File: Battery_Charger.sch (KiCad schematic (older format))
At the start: 27 parts

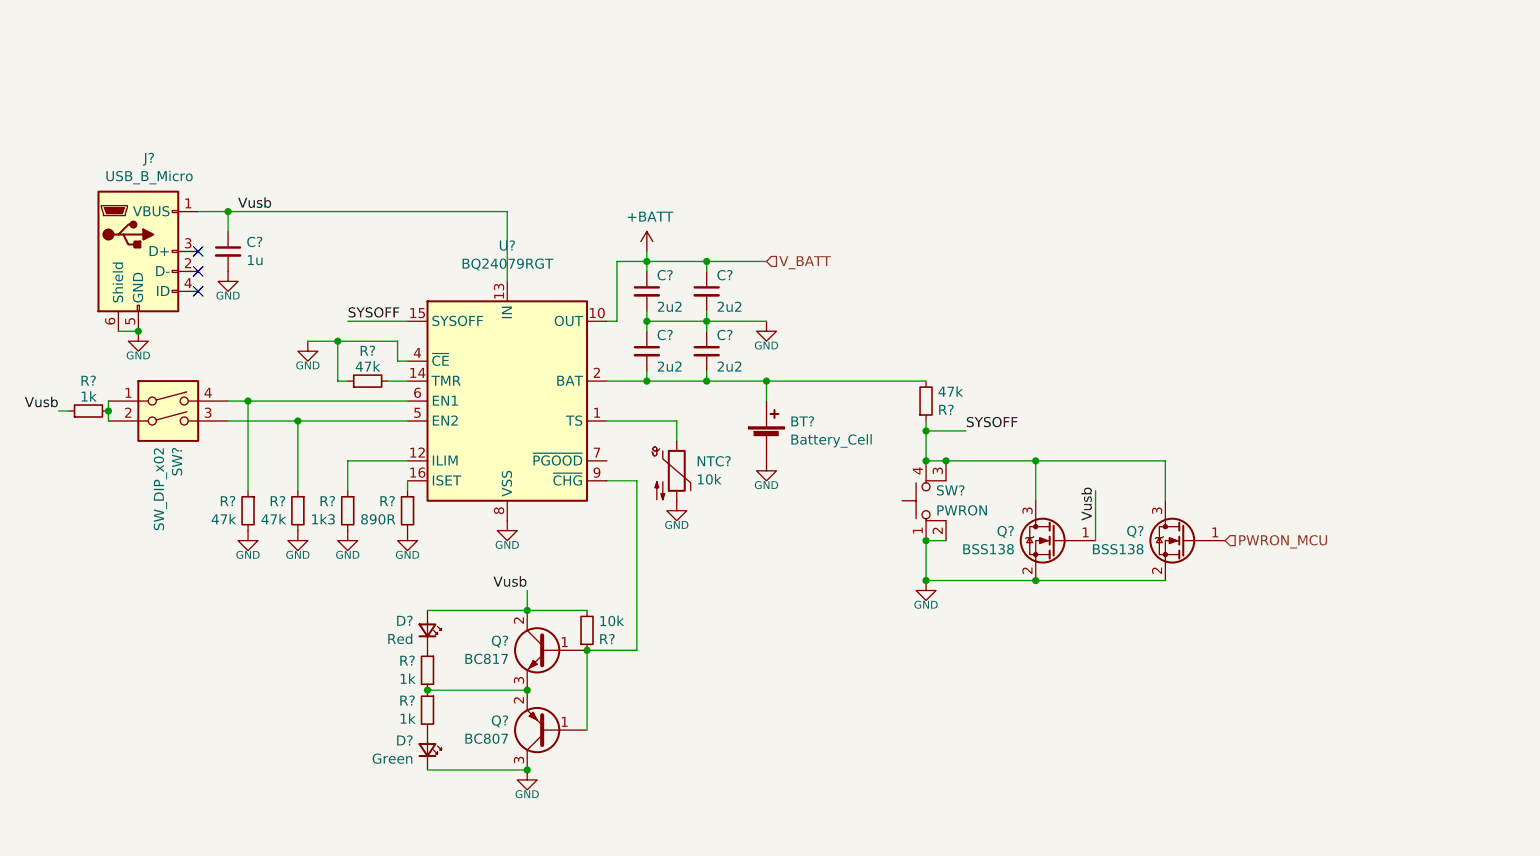
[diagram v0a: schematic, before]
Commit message: - supply converter develop - added sheet: MCU - cleanup 'koncepcja' sub-schematics
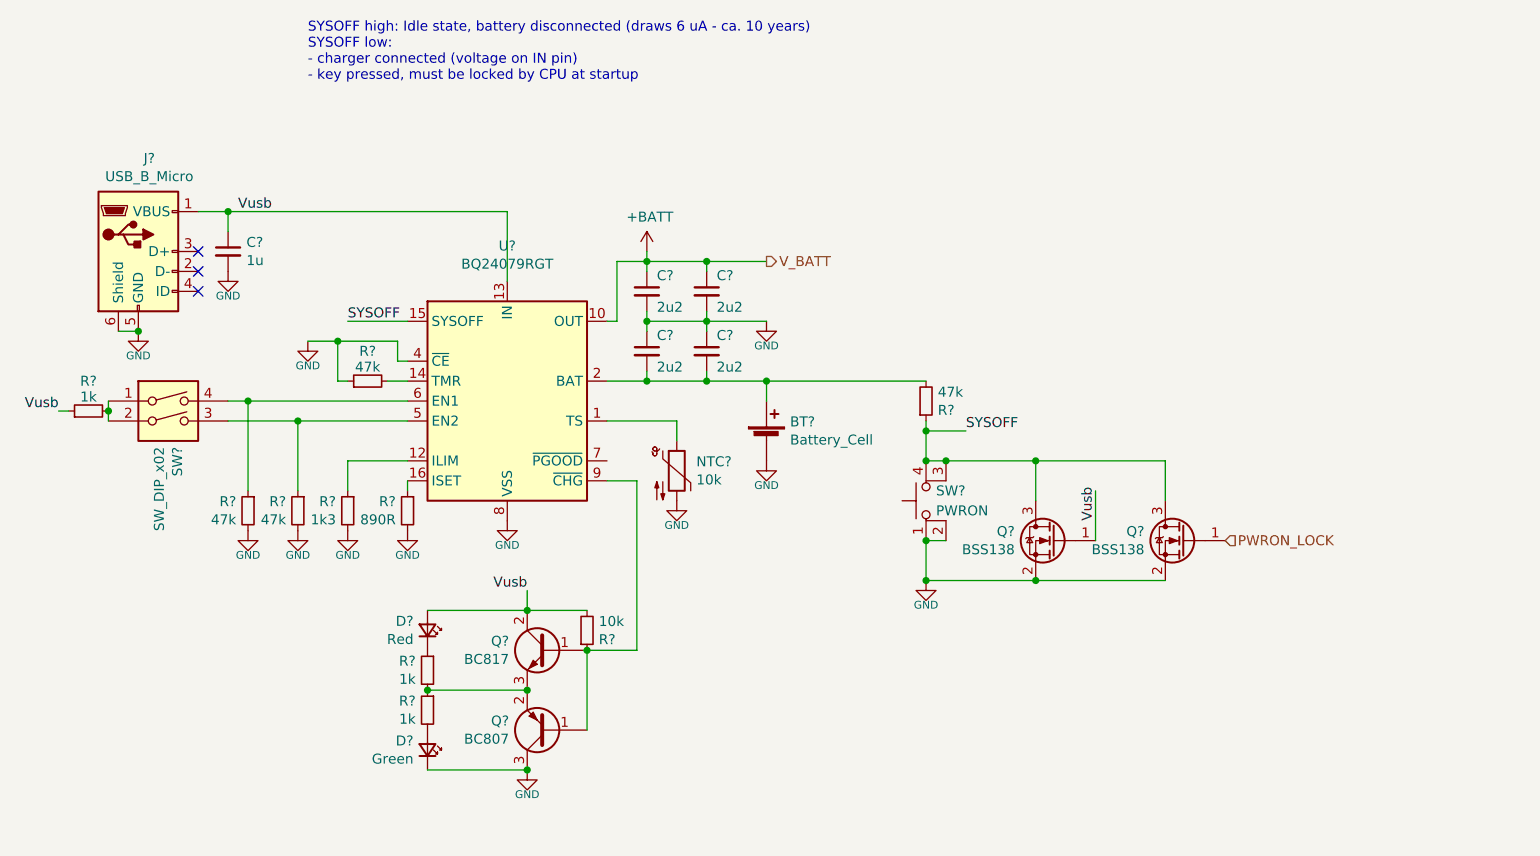
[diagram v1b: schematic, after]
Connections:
- net PWRON_MCU renamed PWRON_LOCK
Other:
- note added: "SYSOFF high: Idle state, battery disconnected (draws 6 uA - ca. 10 years)\nSYSOFF low:\n- charger connected (voltage on IN pin)\n- key pressed, must be locked by CPU at startup"
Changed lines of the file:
@@
 $Descr A4 11693 8268
 encoding utf-8
-Sheet 10 10
+Sheet 10 9
 Title ""
 Date ""
@@
 U 1 1 5F7AA8B0
 P 6150 3600
+AR Path="/5F620813/5F7AA8B0" Ref="BT?"  Part="1"
+AR Path="/5F7A93EE/5F7AA8B0" Ref="BT?"  Part="1"
 F 0 "BT?" H 6268 3696 50  0000 L CNN
 F 1 "Battery_Cell" H 6268 3605 50  0000 L CNN
@@
 U 1 1 5F7AA8B7
 P 4850 3400
+AR Path="/5F620813/5F7AA8B7" Ref="U?"  Part="1"
+AR Path="/5F7A93EE/5F7AA8B7" Ref="U?"  Part="1"
 F 0 "U?" H 4850 4178 50  0000 C CNN
 F 1 "BQ24079RGT" H 4850 4087 50  0000 C CNN
@@
 U 1 1 5F7AA8BE
 P 3000 2650
+AR Path="/5F620813/5F7AA8BE" Ref="J?"  Part="1"
+AR Path="/5F7A93EE/5F7AA8BE" Ref="J?"  Part="1"
 F 0 "J?" H 3055 3117 50  0000 C CNN
 F 1 "USB_B_Micro" H 3055 3026 50  0000 C CNN
@@
 AR Path="/5F7AA8C5" Ref="#PWR?"  Part="1"
 AR Path="/5F620813/5F7AA8C5" Ref="#PWR?"  Part="1"
+AR Path="/5F7A93EE/5F7AA8C5" Ref="#PWR?"  Part="1"
 F 0 "#PWR?" H 3000 2890 50  0001 C CNN
 F 1 "GND" H 3000 2950 39  0000 C TNN
@@
 U 1 1 5F7AA8D1
 P 3450 2650
+AR Path="/5F620813/5F7AA8D1" Ref="C?"  Part="1"
+AR Path="/5F7A93EE/5F7AA8D1" Ref="C?"  Part="1"
 F 0 "C?" H 3542 2696 50  0000 L CNN
 F 1 "1u" H 3542 2605 50  0000 L CNN
@@
 AR Path="/5F7AA8D8" Ref="#PWR?"  Part="1"
 AR Path="/5F620813/5F7AA8D8" Ref="#PWR?"  Part="1"
+AR Path="/5F7A93EE/5F7AA8D8" Ref="#PWR?"  Part="1"
 F 0 "#PWR?" H 3450 2590 50  0001 C CNN
 F 1 "GND" H 3450 2650 39  0000 C TNN
@@
 U 1 1 5F7AA8E8
 P 4450 4550
+AR Path="/5F620813/5F7AA8E8" Ref="D?"  Part="1"
+AR Path="/5F7A93EE/5F7AA8E8" Ref="D?"  Part="1"
 F 0 "D?" V 4496 4480 50  0000 R CNN
 F 1 "Red" V 4405 4480 50  0000 R CNN
@@
 AR Path="/5F7AA8F0" Ref="#PWR?"  Part="1"
 AR Path="/5F620813/5F7AA8F0" Ref="#PWR?"  Part="1"
+AR Path="/5F7A93EE/5F7AA8F0" Ref="#PWR?"  Part="1"
 F 0 "#PWR?" H 4850 3840 50  0001 C CNN
 F 1 "GND" H 4850 3900 39  0000 C TNN
@@
 AR Path="/5F7AA8F6" Ref="#PWR?"  Part="1"
 AR Path="/5F620813/5F7AA8F6" Ref="#PWR?"  Part="1"
+AR Path="/5F7A93EE/5F7AA8F6" Ref="#PWR?"  Part="1"
 F 0 "#PWR?" H 6150 3540 50  0001 C CNN
 F 1 "GND" H 6150 3600 39  0000 C TNN
@@
 AR Path="/5F7AA8FC" Ref="#PWR?"  Part="1"
 AR Path="/5F620813/5F7AA8FC" Ref="#PWR?"  Part="1"
+AR Path="/5F7A93EE/5F7AA8FC" Ref="#PWR?"  Part="1"
 F 0 "#PWR?" H 3850 2940 50  0001 C CNN
 F 1 "GND" H 3850 3000 39  0000 C TNN
@@
 U 1 1 5F7AA902
 P 3150 3500
+AR Path="/5F620813/5F7AA902" Ref="SW?"  Part="1"
+AR Path="/5F7A93EE/5F7AA902" Ref="SW?"  Part="1"
 F 0 "SW?" V 3196 3370 50  0000 R CNN
 F 1 "SW_DIP_x02" V 3105 3370 50  0000 R CNN
@@
 U 1 1 5F7AA90A
 P 4450 5150
+AR Path="/5F620813/5F7AA90A" Ref="D?"  Part="1"
+AR Path="/5F7A93EE/5F7AA90A" Ref="D?"  Part="1"
 F 0 "D?" V 4496 5080 50  0000 R CNN
 F 1 "Green" V 4405 5080 50  0000 R CNN
@@
 U 1 1 5F7AA911
 P 5050 5050
+AR Path="/5F620813/5F7AA911" Ref="Q?"  Part="1"
+AR Path="/5F7A93EE/5F7AA911" Ref="Q?"  Part="1"
 F 0 "Q?" H 5241 5004 50  0000 L CNN
 F 1 "BC807" H 5241 5095 50  0000 L CNN
@@
 U 1 1 5F7AA918
 P 5050 4650
+AR Path="/5F620813/5F7AA918" Ref="Q?"  Part="1"
+AR Path="/5F7A93EE/5F7AA918" Ref="Q?"  Part="1"
 F 0 "Q?" H 5241 4696 50  0000 L CNN
 F 1 "BC817" H 5241 4605 50  0000 L CNN
@@
 AR Path="/5F7AA920" Ref="#PWR?"  Part="1"
 AR Path="/5F620813/5F7AA920" Ref="#PWR?"  Part="1"
+AR Path="/5F7A93EE/5F7AA920" Ref="#PWR?"  Part="1"
 F 0 "#PWR?" H 4950 5090 50  0001 C CNN
 F 1 "GND" H 4950 5150 39  0000 C TNN
@@
 U 1 1 5F7AA927
 P 5250 4550
+AR Path="/5F620813/5F7AA927" Ref="R?"  Part="1"
+AR Path="/5F7A93EE/5F7AA927" Ref="R?"  Part="1"
 F 0 "R?" H 5309 4596 50  0000 L CNN
 F 1 "10k" H 5309 4505 50  0000 L CNN
@@
 AR Path="/5F7AA93D" Ref="#PWR?"  Part="1"
 AR Path="/5F620813/5F7AA93D" Ref="#PWR?"  Part="1"
+AR Path="/5F7A93EE/5F7AA93D" Ref="#PWR?"  Part="1"
 F 0 "#PWR?" H 4350 3890 50  0001 C CNN
 F 1 "GND" H 4350 3950 39  0000 C TNN
@@
 AR Path="/5F7AA943" Ref="#PWR?"  Part="1"
 AR Path="/5F620813/5F7AA943" Ref="#PWR?"  Part="1"
+AR Path="/5F7A93EE/5F7AA943" Ref="#PWR?"  Part="1"
 F 0 "#PWR?" H 4050 3890 50  0001 C CNN
 F 1 "GND" H 4050 3950 39  0000 C TNN
@@
 AR Path="/5F7AA94B" Ref="#PWR?"  Part="1"
 AR Path="/5F620813/5F7AA94B" Ref="#PWR?"  Part="1"
+AR Path="/5F7A93EE/5F7AA94B" Ref="#PWR?"  Part="1"
 F 0 "#PWR?" H 3800 3890 50  0001 C CNN
 F 1 "GND" H 3800 3950 39  0000 C TNN
@@
 U 1 1 5F7AA951
 P 3550 3950
+AR Path="/5F620813/5F7AA951" Ref="R?"  Part="1"
+AR Path="/5F7A93EE/5F7AA951" Ref="R?"  Part="1"
 F 0 "R?" H 3609 3996 50  0000 L CNN
 F 1 "47k" H 3609 3905 50  0000 L CNN
@@
 AR Path="/5F7AA958" Ref="#PWR?"  Part="1"
 AR Path="/5F620813/5F7AA958" Ref="#PWR?"  Part="1"
+AR Path="/5F7A93EE/5F7AA958" Ref="#PWR?"  Part="1"
 F 0 "#PWR?" H 3550 3890 50  0001 C CNN
 F 1 "GND" H 3550 3950 39  0000 C TNN
@@
 U 1 1 5F7AA968
 P 3800 3950
+AR Path="/5F620813/5F7AA968" Ref="R?"  Part="1"
+AR Path="/5F7A93EE/5F7AA968" Ref="R?"  Part="1"
 F 0 "R?" H 3859 3996 50  0000 L CNN
 F 1 "47k" H 3859 3905 50  0000 L CNN
@@
 U 1 1 5F7AA96F
 P 4050 3950
+AR Path="/5F620813/5F7AA96F" Ref="R?"  Part="1"
+AR Path="/5F7A93EE/5F7AA96F" Ref="R?"  Part="1"
 F 0 "R?" H 4109 3996 50  0000 L CNN
 F 1 "1k3" H 4109 3905 50  0000 L CNN
@@
 U 1 1 5F7AA976
 P 4350 3950
+AR Path="/5F620813/5F7AA976" Ref="R?"  Part="1"
+AR Path="/5F7A93EE/5F7AA976" Ref="R?"  Part="1"
 F 0 "R?" H 4409 3996 50  0000 L CNN
 F 1 "890R" H 4409 3905 50  0000 L CNN
@@
 U 1 1 5F7AA97D
 P 4450 4750
+AR Path="/5F620813/5F7AA97D" Ref="R?"  Part="1"
+AR Path="/5F7A93EE/5F7AA97D" Ref="R?"  Part="1"
 F 0 "R?" H 4509 4796 50  0000 L CNN
 F 1 "1k" H 4509 4705 50  0000 L CNN
@@
 U 1 1 5F7AA984
 P 4450 4950
+AR Path="/5F620813/5F7AA984" Ref="R?"  Part="1"
+AR Path="/5F7A93EE/5F7AA984" Ref="R?"  Part="1"
 F 0 "R?" H 4509 4996 50  0000 L CNN
 F 1 "1k" H 4509 4905 50  0000 L CNN
@@
 U 1 1 5F7AA98C
 P 2750 3450
+AR Path="/5F620813/5F7AA98C" Ref="R?"  Part="1"
+AR Path="/5F7A93EE/5F7AA98C" Ref="R?"  Part="1"
 F 0 "R?" V 2900 3450 50  0000 C CNN
 F 1 "1k" V 2850 3450 50  0000 C BNN
@@
 U 1 1 5F7AA998
 P 5700 3750
+AR Path="/5F620813/5F7AA998" Ref="NTC?"  Part="1"
+AR Path="/5F7A93EE/5F7AA998" Ref="NTC?"  Part="1"
 F 0 "NTC?" H 5798 3796 50  0000 L CNN
 F 1 "10k" H 5798 3705 50  0000 L CNN
@@
 AR Path="/5F7AA9A1" Ref="#PWR?"  Part="1"
 AR Path="/5F620813/5F7AA9A1" Ref="#PWR?"  Part="1"
+AR Path="/5F7A93EE/5F7AA9A1" Ref="#PWR?"  Part="1"
 F 0 "#PWR?" H 5700 3740 50  0001 C CNN
 F 1 "GND" H 5700 3800 39  0000 C TNN
@@
 U 1 1 5F7AA9A7
 P 5550 3150
+AR Path="/5F620813/5F7AA9A7" Ref="C?"  Part="1"
+AR Path="/5F7A93EE/5F7AA9A7" Ref="C?"  Part="1"
 F 0 "C?" H 5600 3200 50  0000 L BNN
 F 1 "2u2" H 5600 3100 50  0000 L TNN
@@
 U 1 1 5F7AA9AE
 P 5550 2850
+AR Path="/5F620813/5F7AA9AE" Ref="C?"  Part="1"
+AR Path="/5F7A93EE/5F7AA9AE" Ref="C?"  Part="1"
 F 0 "C?" H 5600 2900 50  0000 L BNN
 F 1 "2u2" H 5600 2800 50  0000 L TNN
@@
 U 1 1 5F7AA9B5
 P 5850 3150
+AR Path="/5F620813/5F7AA9B5" Ref="C?"  Part="1"
+AR Path="/5F7A93EE/5F7AA9B5" Ref="C?"  Part="1"
 F 0 "C?" H 5900 3200 50  0000 L BNN
 F 1 "2u2" H 5900 3100 50  0000 L TNN
@@
 U 1 1 5F7AA9BC
 P 5850 2850
+AR Path="/5F620813/5F7AA9BC" Ref="C?"  Part="1"
+AR Path="/5F7A93EE/5F7AA9BC" Ref="C?"  Part="1"
 F 0 "C?" H 5900 2900 50  0000 L BNN
 F 1 "2u2" H 5900 2800 50  0000 L TNN
@@
 AR Path="/5F7AA9C3" Ref="#PWR?"  Part="1"
 AR Path="/5F620813/5F7AA9C3" Ref="#PWR?"  Part="1"
+AR Path="/5F7A93EE/5F7AA9C3" Ref="#PWR?"  Part="1"
 F 0 "#PWR?" H 6150 2840 50  0001 C CNN
 F 1 "GND" H 6150 2900 39  0000 C TNN
@@
 U 1 1 5F7AA9DF
 P 7050 3900
+AR Path="/5F620813/5F7AA9DF" Ref="SW?"  Part="1"
+AR Path="/5F7A93EE/5F7AA9DF" Ref="SW?"  Part="1"
 F 0 "SW?" V 7100 3950 50  0000 R CNN
 F 1 "PWRON" V 7000 3950 50  0000 R CNN
@@
 U 1 1 5F7AA9E6
 P 4150 3300
+AR Path="/5F620813/5F7AA9E6" Ref="R?"  Part="1"
+AR Path="/5F7A93EE/5F7AA9E6" Ref="R?"  Part="1"
 F 0 "R?" V 4300 3300 50  0000 C CNN
 F 1 "47k" V 4250 3300 50  0000 C BNN
@@
 U 1 1 5F7AA9F5
 P 6950 3400
+AR Path="/5F620813/5F7AA9F5" Ref="R?"  Part="1"
+AR Path="/5F7A93EE/5F7AA9F5" Ref="R?"  Part="1"
 F 0 "R?" H 7009 3446 50  0000 L CNN
 F 1 "47k" H 7009 3355 50  0000 L CNN
@@
 AR Path="/5F7AAA05" Ref="#PWR?"  Part="1"
 AR Path="/5F620813/5F7AAA05" Ref="#PWR?"  Part="1"
+AR Path="/5F7A93EE/5F7AAA05" Ref="#PWR?"  Part="1"
 F 0 "#PWR?" H 6950 4140 50  0001 C CNN
 F 1 "GND" H 6950 4200 39  0000 C TNN
@@
 U 1 1 5F7AAA0C
 P 7600 4100
+AR Path="/5F620813/5F7AAA0C" Ref="Q?"  Part="1"
+AR Path="/5F7A93EE/5F7AAA0C" Ref="Q?"  Part="1"
 F 0 "Q?" H 7805 4146 50  0000 L CNN
 F 1 "BSS138" H 7805 4055 50  0000 L CNN
@@
 U 1 1 5F7AAA19
 P 8250 4100
+AR Path="/5F620813/5F7AAA19" Ref="Q?"  Part="1"
+AR Path="/5F7A93EE/5F7AAA19" Ref="Q?"  Part="1"
 F 0 "Q?" H 8455 4146 50  0000 L CNN
 F 1 "BSS138" H 8455 4055 50  0000 L CNN
@@
 	8150 3900 8150 3700
 Text HLabel 8450 4100 2    50   Input ~ 0
-PWRON_MCU
+PWRON_LOCK
 Text Label 7800 4000 1    50   ~ 0
 Vusb
@@
 	1    0    0    -1
 $EndComp
-Text HLabel 6150 2700 2    50   Input ~ 0
+Text HLabel 6150 2700 2    50   Output ~ 0
 V_BATT
 Wire Wire Line
 	6150 2700 5850 2700
 Connection ~ 5850 2700
+Text Notes 3850 1800 0    50   ~ 0
+SYSOFF high: Idle state, battery disconnected (draws 6 uA - ca. 10 years)\nSYSOFF low:\n- charger connected (voltage on IN pin)\n- key pressed, must be locked by CPU at startup
 $EndSCHEMATC

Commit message: - added footprint & 3D model of DC/DC HV converter - updated battery (to 2x battery holder) - some changes in supply
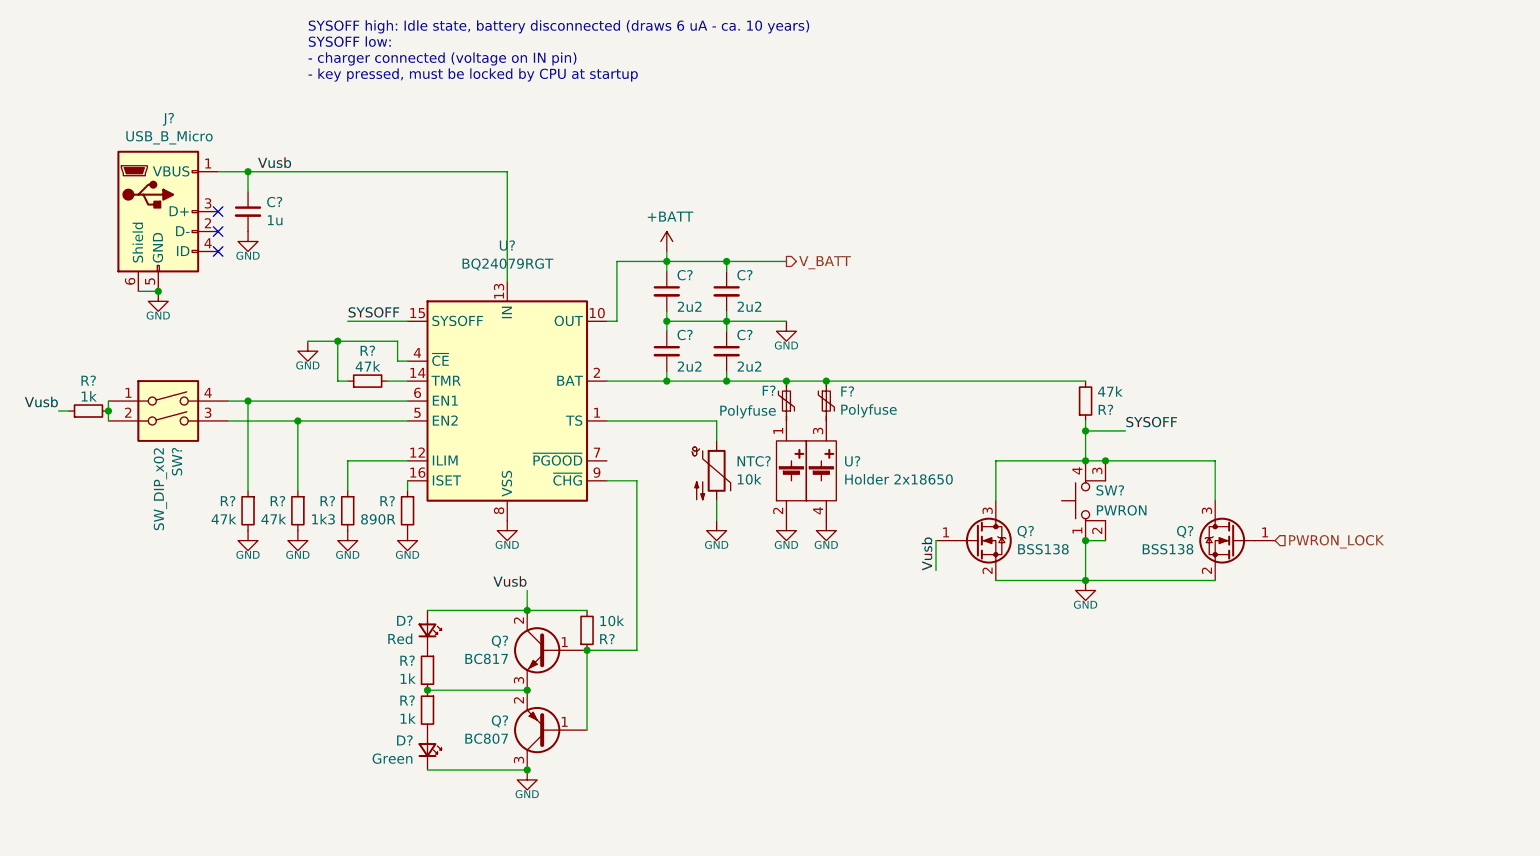
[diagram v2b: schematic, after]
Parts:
- removed BT?: Battery_Cell, symbol Device:Battery_Cell
- added F? (x2): Polyfuse, symbol Device:Polyfuse_Small
- added U?: Holder 2x18650, symbol battery:Eagle_12BHC186P
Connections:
- net GND: now also U?.2 (1-), U?.4 (2-)
- net at C?.2, C?.2, R?.2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: now also F?.1, F?.2
- new net: F?.1, U?.1 (1+)
- new net: F?.2, U?.3 (2+)
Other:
- moved on the sheet: C?, J?, NTC?, Q?, R?, SW?
